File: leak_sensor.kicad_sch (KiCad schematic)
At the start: 4 parts, among them J9 TLW-104-05-T-D, Q4 TP2104N3-G

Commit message: Cleanup symbol field table
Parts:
- J9: ALTIUM_VALUE 2x4 -> (none); LATESTREVISIONDATE 17-Jul-2002 -> (none); LATESTREVISIONNOTE Re-released for DXP Platform. -> (none); MANUFACTURER Samtec Inc. -> (none); MANUFACTURER PART NUMBER TLW-104-05-T-D -> (none); PUBLISHER Altium Limited -> (none); Part Number (none) -> TLW-104-05-T-D
- Q4: ALTIUM_VALUE 20V -> (none); CASE/PACKAGE TO-92-3 -> (none); CONTINUOUS DRAIN CURRENT (ID) 175mA -> (none); DRAIN TO SOURCE BREAKDOWN VOLTAGE -40V -> (none); DRAIN TO SOURCE RESISTANCE 6R -> (none); DRAIN TO SOURCE VOLTAGE (VDSS) 40V -> (none); ELEMENT CONFIGURATION Single -> (none); FALL TIME 4ns -> (none); GATE TO SOURCE VOLTAGE (VGS) 20V -> (none); HEIGHT 5.33mm -> (none); INPUT CAPACITANCE 60pF -> (none); LEAD FREE Lead Free -> (none); LENGTH 5.21mm -> (none); MANUFACTURER Microchip Technology -> (none); MANUFACTURER PART NUMBER TP2104N3-G -> (none); MAX OPERATING TEMPERATURE 150°C -> (none); MAX POWER DISSIPATION 740mW -> (none); MIN OPERATING TEMPERATURE -55°C -> (none); MOUNT Through Hole -> (none); NUMBER OF CHANNELS 1 -> (none); NUMBER OF PINS 3 -> (none); PACKAGE QUANTITY 1000 -> (none); PACKAGING Bulk -> (none); POLARITY P-CHANNEL -> (none); POWER DISSIPATION 740mW -> (none); Part Number (none) -> TP2104N3-G; RDS ON MAX 6R -> (none); RISE TIME 4ns -> (none); ROHS COMPLIANT Yes -> (none); SERIES - -> (none); TURN-OFF DELAY TIME 5ns -> (none); TURN-ON DELAY TIME 4ns -> (none); WEIGHT 0.016oz -> (none); WIDTH 4.19mm -> (none)
- R15: ALTIUM_VALUE 1M -> (none); CASE CODE (IMPERIAL) 0805 -> (none); CASE CODE (METRIC) 2012 -> (none); CASE/PACKAGE 0805 -> (none); CONSTRUCTION Rectangular -> (none); CONTACT PLATING Tin -> (none); DEPTH 1.25mm -> (none); FEATURES Automotive AEC-Q200 -> (none); HEIGHT 0.026inch -> (none); LEAD FREE Lead Free -> (none); LENGTH 2mm -> (none); MANUFACTURER Stackpole Electronics Inc -> (none); MANUFACTURER PART NUMBER RMCF0805JT1M00 -> (none); MAX OPERATING TEMPERATURE 155°C -> (none); MAX POWER DISSIPATION 125mW -> (none); MILITARY STANDARD Not -> (none); MIN OPERATING TEMPERATURE -55°C -> (none); MOUNT Surface Mount -> (none); NUMBER OF TERMINATIONS 2 -> (none); PACKAGING Tape and Reel -> (none); Part Number (none) -> RMCF0805JT1M00; RADIATION HARDENING No -> (none); RESISTANCE 1MR -> (none); RESISTOR TYPE Thick Film -> (none); ROHS COMPLIANT Yes -> (none); SERIES RMCF -> (none); TEMPERATURE COEFFICIENT 200ppm/°C -> (none); TOLERANCE 5% -> (none); WIDTH 0.049inch -> (none)
- R16: ALTIUM_VALUE 10k -> (none); CASE CODE (IMPERIAL) 0805 -> (none); CASE CODE (METRIC) 2012 -> (none); CASE/PACKAGE 0805 -> (none); FEATURES Moisture Resistant -> (none); HEIGHT 0.024inch -> (none); LEAD FREE Lead Free -> (none); LENGTH 0.079inch -> (none); MANUFACTURER Stackpole Electronics Inc -> (none); MANUFACTURER PART NUMBER RNCP0805FTD10K0 -> (none); MAX OPERATING TEMPERATURE 155°C -> (none); MAX POWER DISSIPATION 250mW -> (none); MIN OPERATING TEMPERATURE -55°C -> (none); MOUNT Surface Mount -> (none); NUMBER OF TERMINATIONS 2 -> (none); PACKAGING Tape and Reel -> (none); Part Number (none) -> RNCP0805FTD10K0; RESISTANCE 10kR -> (none); RESISTOR TYPE Thin Film -> (none); ROHS COMPLIANT Yes -> (none); SERIES RNCP -> (none); TEMPERATURE COEFFICIENT 100ppm/°C -> (none); TOLERANCE 1% -> (none); WIDTH 0.049inch -> (none)

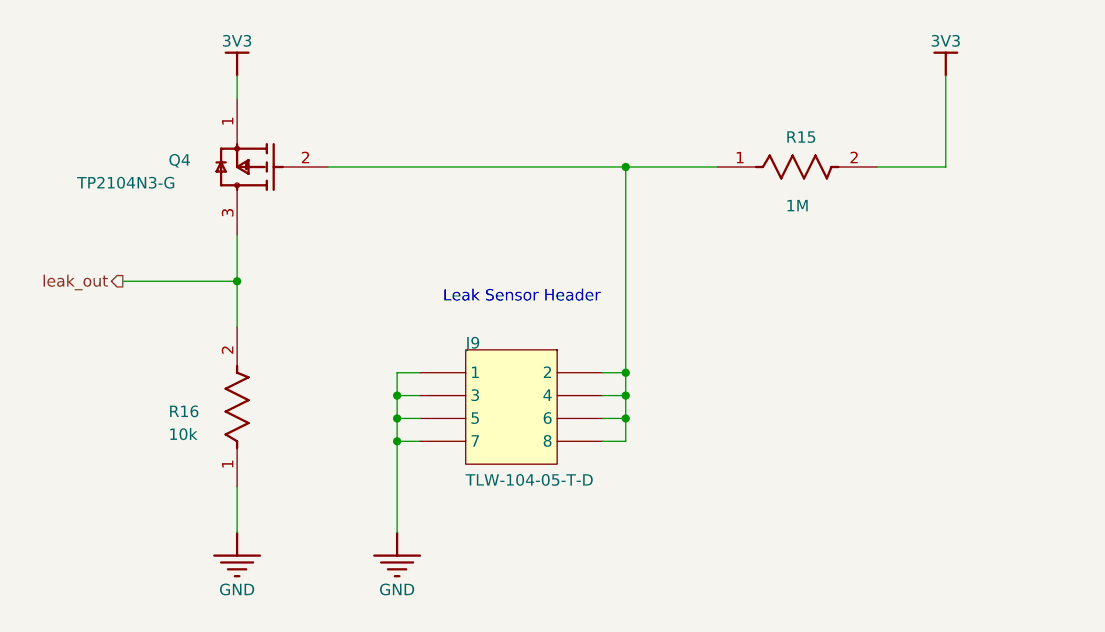
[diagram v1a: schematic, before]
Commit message: Input and Output Header Updates to MEB
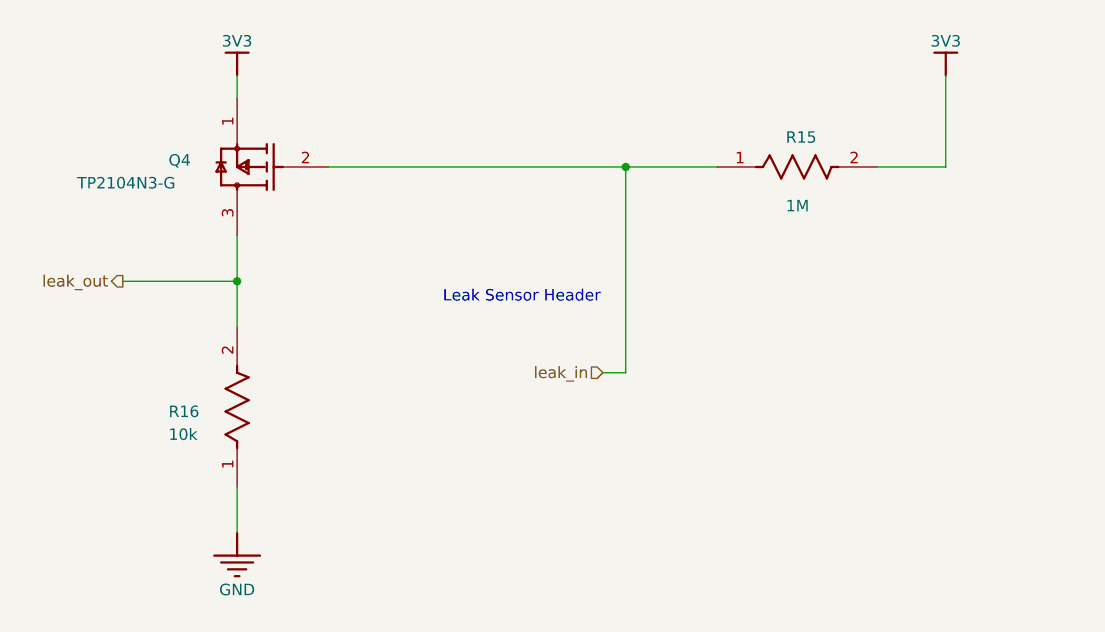
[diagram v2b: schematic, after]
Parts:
- removed J9: TLW-104-05-T-D, AltiumImport:HDR2X4, symbol MEB-altium-import:leak_sensor_0_Header 4X2
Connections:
- net leak_in: now reaches Q4.2 (Gate), R15.1
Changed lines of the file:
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@@
   (junction (at 81.28 101.6) (diameter 0) (color 0 0 0 0)
   )
-  (junction (at 124.46 114.3) (diameter 0) (color 0 0 0 0)
-  )
-  (junction (at 99.06 116.84) (diameter 0) (color 0 0 0 0)
-  )
-  (junction (at 99.06 119.38) (diameter 0) (color 0 0 0 0)
-  )
-  (junction (at 99.06 114.3) (diameter 0) (color 0 0 0 0)
-  )
   (junction (at 124.46 88.9) (diameter 0) (color 0 0 0 0)
-  )
-  (junction (at 124.46 111.76) (diameter 0) (color 0 0 0 0)
-  )
-  (junction (at 124.46 116.84) (diameter 0) (color 0 0 0 0)
   )
   (wire (pts (xy 124.46 88.9) (xy 124.46 111.76))
     (stroke (width 0.254) (type default))
   )
-  (wire (pts (xy 99.06 111.76) (xy 99.06 114.3))
-    (stroke (width 0.254) (type default))
-  )
-  (wire (pts (xy 124.46 116.84) (xy 124.46 119.38))
-    (stroke (width 0.254) (type default))
-  )
-  (wire (pts (xy 101.6 111.76) (xy 99.06 111.76))
-    (stroke (width 0.254) (type default))
-  )
-  (wire (pts (xy 99.06 114.3) (xy 101.6 114.3))
-    (stroke (width 0.254) (type default))
-  )
-  (wire (pts (xy 124.46 114.3) (xy 124.46 116.84))
-    (stroke (width 0.254) (type default))
-  )
-  (wire (pts (xy 101.6 116.84) (xy 99.06 116.84))
-    (stroke (width 0.254) (type default))
-  )
-  (wire (pts (xy 121.92 116.84) (xy 124.46 116.84))
-    (stroke (width 0.254) (type default))
-  )
   (wire (pts (xy 81.28 129.54) (xy 81.28 124.46))
-    (stroke (width 0.254) (type default))
-  )
-  (wire (pts (xy 124.46 111.76) (xy 124.46 114.3))
     (stroke (width 0.254) (type default))
   )
@@
   )
   (wire (pts (xy 160.02 78.74) (xy 160.02 88.9))
-    (stroke (width 0.254) (type default))
-  )
-  (wire (pts (xy 124.46 119.38) (xy 121.92 119.38))
-    (stroke (width 0.254) (type default))
-  )
-  (wire (pts (xy 99.06 119.38) (xy 99.06 129.54))
     (stroke (width 0.254) (type default))
   )
@@
     (stroke (width 0.254) (type default))
   )
-  (wire (pts (xy 99.06 114.3) (xy 99.06 116.84))
-    (stroke (width 0.254) (type default))
-  )
-  (wire (pts (xy 99.06 119.38) (xy 101.6 119.38))
-    (stroke (width 0.254) (type default))
-  )
   (wire (pts (xy 81.28 78.74) (xy 81.28 81.28))
-    (stroke (width 0.254) (type default))
-  )
-  (wire (pts (xy 124.46 114.3) (xy 121.92 114.3))
-    (stroke (width 0.254) (type default))
-  )
-  (wire (pts (xy 99.06 116.84) (xy 99.06 119.38))
     (stroke (width 0.254) (type default))
   )
@@
     (effects (font (size 1.27 1.27)) (justify right))
   )
-  (symbol (lib_id "MEB-altium-import:leak_sensor_0_Header 4X2") (at 106.68 109.22 0) (unit 1)
-    (in_bom yes) (on_board yes) (dnp no)
-    (property "Reference" "J9" (at 106.68 109.22 0)
-      (effects (font (size 1.27 1.27)) (justify left bottom))
-    )
-    (property "Value" "TLW-104-05-T-D" (at 106.68 124.46 0)
-      (effects (font (size 1.27 1.27)) (justify left bottom))
-    )
-    (property "Footprint" "AltiumImport:HDR2X4" (at 106.68 109.22 0)
-      (effects (font (size 1.27 1.27)) hide)
-    )
-    (property "Datasheet" "" (at 106.68 109.22 0)
-      (effects (font (size 1.27 1.27)) hide)
-    )
-    (property "Part Number" "TLW-104-05-T-D" (at 106.68 109.22 0)
-      (effects (font (size 1.27 1.27)) hide)
-    )
-    (pin "1")
-    (pin "2")
-    (pin "3")
-    (pin "4")
-    (pin "5")
-    (pin "6")
-    (pin "7")
-    (pin "8")
-    (instances
-      (project "MEB"
-        (path "/228e4997-23c1-4c21-939b-583cad26a5e3/0dfd1422-c5d3-49c9-a73a-0802f4b457f4"
-          (reference "J9") (unit 1)
-        )
-      )
-    )
+  (hierarchical_label "leak_in" (shape input) (at 121.92 111.76 180) (fields_autoplaced)
+    (effects (font (size 1.27 1.27)) (justify right))
   )
   (symbol (lib_id "MEB-altium-import:leak_sensor_1_1029c3af85768c4190bb7ad29bc67b5") (at 81.28 124.46 0) (unit 1)
@@
         )
       )
-    )
-  )
-  (symbol (lib_id "MEB-altium-import:GND") (at 99.06 129.54 0) (unit 1)
-    (in_bom yes) (on_board yes) (dnp no)
-    (property "Reference" "#PWR0109" (at 99.06 129.54 0)
-      (effects (font (size 1.27 1.27)) hide)
-    )
-    (property "Value" "GND" (at 99.06 135.89 0)
-      (effects (font (size 1.27 1.27)))
-    )
-    (property "Footprint" "" (at 99.06 129.54 0)
-      (effects (font (size 1.27 1.27)) hide)
-    )
-    (property "Datasheet" "" (at 99.06 129.54 0)
-      (effects (font (size 1.27 1.27)) hide)
-    )
-    (pin "")
-    (instances
-      (project "MEB"
-        (path "/228e4997-23c1-4c21-939b-583cad26a5e3/0dfd1422-c5d3-49c9-a73a-0802f4b457f4"
-          (reference "#PWR0109") (unit 1)
-        )
-      )

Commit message: Finalized schematic and began assigning footprints
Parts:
- R15: footprint AltiumImport:FP-RMCF0805-IPC_C -> Resistor_SMD:R_0805_2012Metric_Pad1.20x1.40mm_HandSolder
- R16: footprint AltiumImport:FP-RNCP0805-IPC_C -> Resistor_SMD:R_0805_2012Metric_Pad1.20x1.40mm_HandSolder
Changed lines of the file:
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@@
       (effects (font (size 1.27 1.27)) (justify left bottom))
     )
-    (property "Footprint" "AltiumImport:FP-RNCP0805-IPC_C" (at 81.28 124.46 0)
+    (property "Footprint" "Resistor_SMD:R_0805_2012Metric_Pad1.20x1.40mm_HandSolder" (at 81.28 124.46 0)
       (effects (font (size 1.27 1.27)) hide)
     )
@@
       (effects (font (size 1.27 1.27)) (justify left bottom))
     )
-    (property "Footprint" "AltiumImport:FP-RMCF0805-IPC_C" (at 134.62 88.9 0)
+    (property "Footprint" "Resistor_SMD:R_0805_2012Metric_Pad1.20x1.40mm_HandSolder" (at 134.62 88.9 0)
       (effects (font (size 1.27 1.27)) hide)
     )

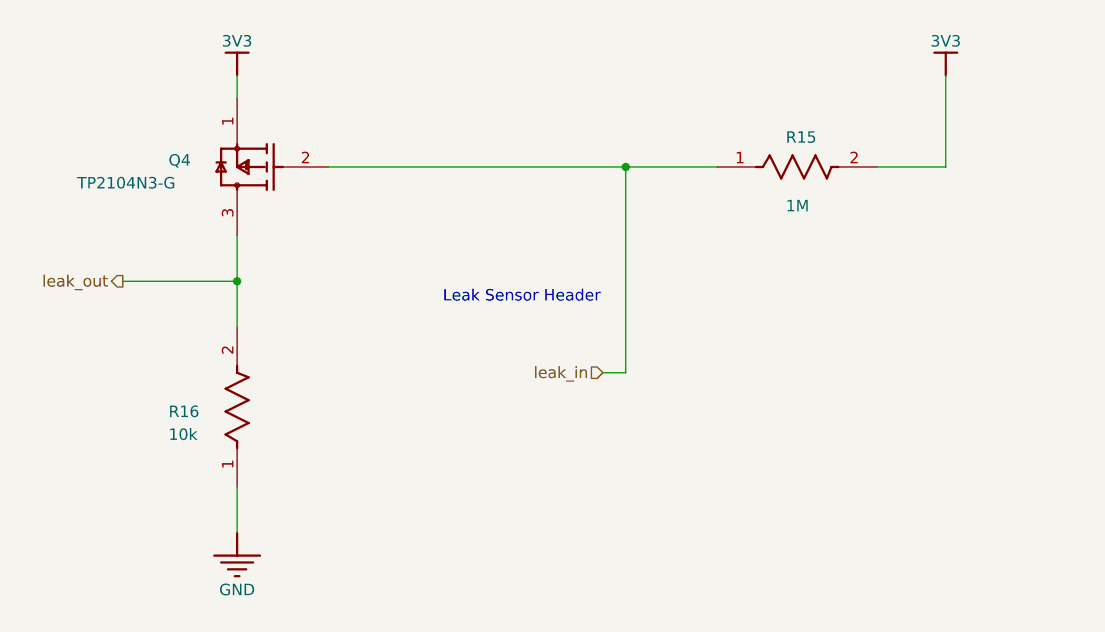
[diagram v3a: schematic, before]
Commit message: updated power and ground symbols in schematic to kicad library version
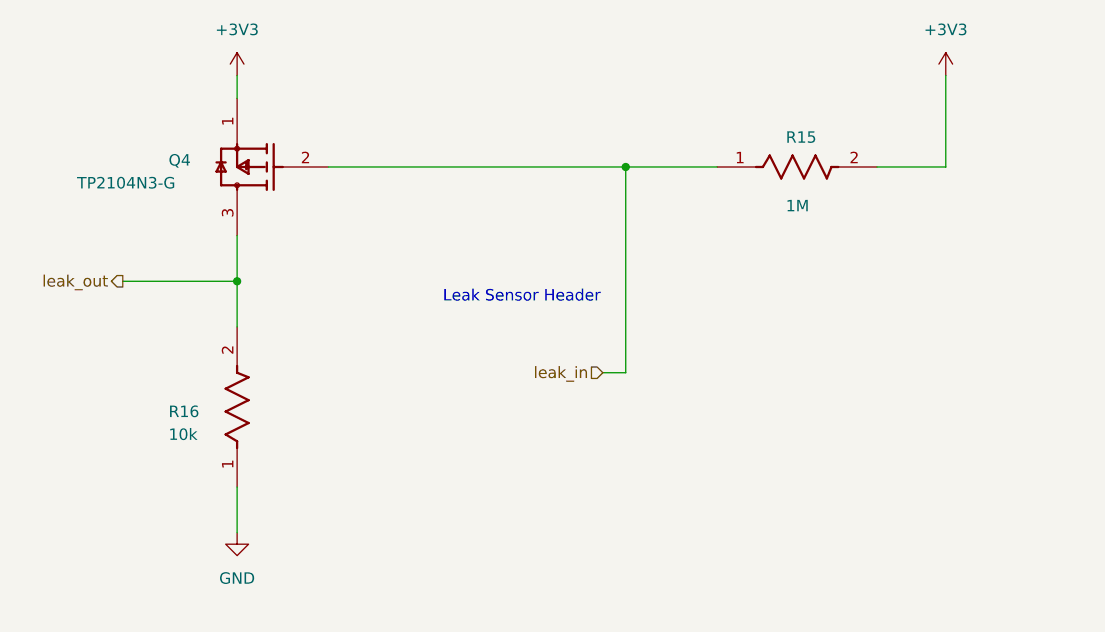
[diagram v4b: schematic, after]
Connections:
- net 3V3 renamed +3V3
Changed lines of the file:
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@@
+    )
+  )
+  (symbol (lib_id "power:GND") (at 81.28 129.54 0) (unit 1)
+    (in_bom yes) (on_board yes) (dnp no) (fields_autoplaced)
+    (property "Reference" "#PWR030" (at 81.28 135.89 0)
+      (effects (font (size 1.27 1.27)) hide)
+    )
+    (property "Value" "GND" (at 81.28 134.62 0)
+      (effects (font (size 1.27 1.27)))
+    )
+    (property "Footprint" "" (at 81.28 129.54 0)
+      (effects (font (size 1.27 1.27)) hide)
+    )
+    (property "Datasheet" "" (at 81.28 129.54 0)
+      (effects (font (size 1.27 1.27)) hide)
+    )
+    (pin "1")
+    (instances
+      (project "MEB"
+        (path "/228e4997-23c1-4c21-939b-583cad26a5e3/3aab6a70-cc66-4393-a750-92acad576aaa"
+          (reference "#PWR030") (unit 1)
+        )
+        (path "/228e4997-23c1-4c21-939b-583cad26a5e3/0dfd1422-c5d3-49c9-a73a-0802f4b457f4"
+          (reference "#PWR027") (unit 1)
+        )
+      )
     )
   )
@@
     )
   )
-  (symbol (lib_id "MEB-altium-import:3V3") (at 160.02 78.74 180) (unit 1)
-    (in_bom yes) (on_board yes) (dnp no)
-    (property "Reference" "#PWR0111" (at 160.02 78.74 0)
+  (symbol (lib_id "power:+3V3") (at 81.28 78.74 0) (unit 1)
+    (in_bom yes) (on_board yes) (dnp no) (fields_autoplaced)
+    (property "Reference" "#PWR036" (at 81.28 82.55 0)
       (effects (font (size 1.27 1.27)) hide)
     )
-    (property "Value" "3V3" (at 160.02 74.93 0)
+    (property "Value" "+3V3" (at 81.28 73.66 0)
+      (effects (font (size 1.27 1.27)))
+    )
+    (property "Footprint" "" (at 81.28 78.74 0)
+      (effects (font (size 1.27 1.27)) hide)
+    )
+    (property "Datasheet" "" (at 81.28 78.74 0)
+      (effects (font (size 1.27 1.27)) hide)
+    )
+    (pin "1")
+    (instances
+      (project "MEB"
+        (path "/228e4997-23c1-4c21-939b-583cad26a5e3"
+          (reference "#PWR036") (unit 1)
+        )
+        (path "/228e4997-23c1-4c21-939b-583cad26a5e3/0dfd1422-c5d3-49c9-a73a-0802f4b457f4"
+          (reference "#PWR037") (unit 1)
+        )
+      )
+    )
+  )
+  (symbol (lib_id "power:+3V3") (at 160.02 78.74 0) (unit 1)
+    (in_bom yes) (on_board yes) (dnp no) (fields_autoplaced)
+    (property "Reference" "#PWR036" (at 160.02 82.55 0)
+      (effects (font (size 1.27 1.27)) hide)
+    )
+    (property "Value" "+3V3" (at 160.02 73.66 0)
       (effects (font (size 1.27 1.27)))
     )
@@
       (effects (font (size 1.27 1.27)) hide)
     )
-    (pin "")
+    (pin "1")
     (instances
       (project "MEB"
+        (path "/228e4997-23c1-4c21-939b-583cad26a5e3"
+          (reference "#PWR036") (unit 1)
+        )
         (path "/228e4997-23c1-4c21-939b-583cad26a5e3/0dfd1422-c5d3-49c9-a73a-0802f4b457f4"
-          (reference "#PWR0111") (unit 1)
+          (reference "#PWR038") (unit 1)
         )
       )
-    )
-  )
-  (symbol (lib_id "MEB-altium-import:GND") (at 81.28 129.54 0) (unit 1)
-    (in_bom yes) (on_board yes) (dnp no)
-    (property "Reference" "#PWR0110" (at 81.28 129.54 0)
-      (effects (font (size 1.27 1.27)) hide)
-    )
-    (property "Value" "GND" (at 81.28 135.89 0)
-      (effects (font (size 1.27 1.27)))
-    )
-    (property "Footprint" "" (at 81.28 129.54 0)
-      (effects (font (size 1.27 1.27)) hide)
-    )
-    (property "Datasheet" "" (at 81.28 129.54 0)
-      (effects (font (size 1.27 1.27)) hide)
-    )
-    (pin "")
-    (instances
-      (project "MEB"
-        (path "/228e4997-23c1-4c21-939b-583cad26a5e3/0dfd1422-c5d3-49c9-a73a-0802f4b457f4"
-          (reference "#PWR0110") (unit 1)
-        )
-      )
-    )
-  )
-  (symbol (lib_id "MEB-altium-import:3V3") (at 81.28 78.74 180) (unit 1)
-    (in_bom yes) (on_board yes) (dnp no)
-    (property "Reference" "#PWR0112" (at 81.28 78.74 0)
-      (effects (font (size 1.27 1.27)) hide)
-    )
-    (property "Value" "3V3" (at 81.28 74.93 0)
-      (effects (font (size 1.27 1.27)))
-    )
-    (property "Footprint" "" (at 81.28 78.74 0)
-      (effects (font (size 1.27 1.27)) hide)
-    )
-    (property "Datasheet" "" (at 81.28 78.74 0)
-      (effects (font (size 1.27 1.27)) hide)
-    )
-    (pin "")
-    (instances
-      (project "MEB"
-        (path "/228e4997-23c1-4c21-939b-583cad26a5e3/0dfd1422-c5d3-49c9-a73a-0802f4b457f4"
-          (reference "#PWR0112") (unit 1)
-        )
-      )
